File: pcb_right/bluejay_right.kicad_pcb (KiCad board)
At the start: 2 copper layers, 147 x 140.5 mm, 70 parts, among them J2 SJ-43514, U2 MCP23017

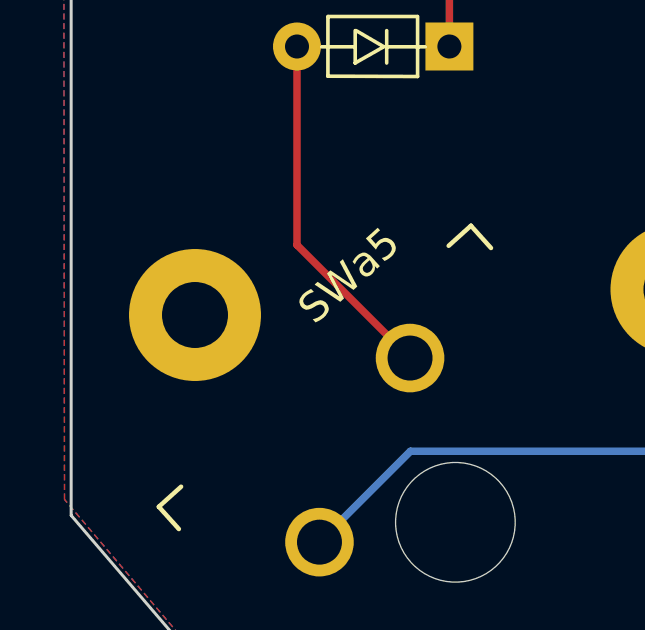
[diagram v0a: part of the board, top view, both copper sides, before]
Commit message: remove mounting hole 9
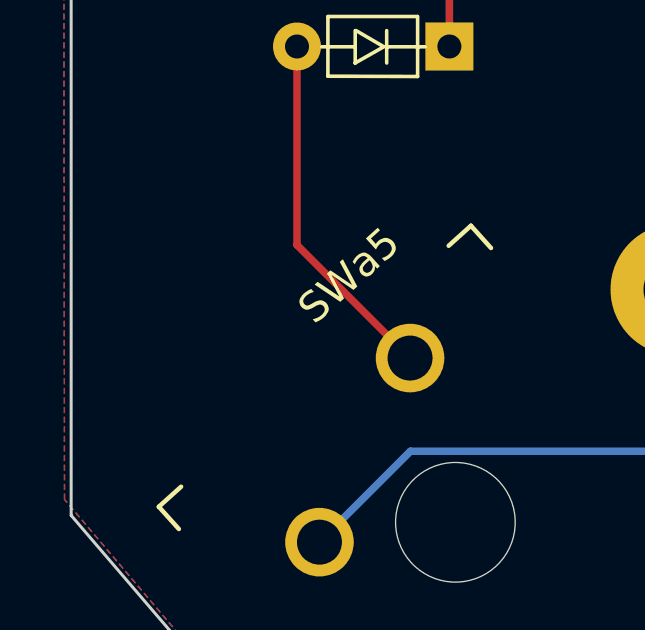
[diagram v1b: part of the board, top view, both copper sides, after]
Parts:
- removed H9: M2, MountingHole:MountingHole_2.2mm_M2_Pad
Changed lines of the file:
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@@
     )
-  )
-  (footprint "MountingHole:MountingHole_2.2mm_M2_Pad" (layer "F.Cu")
-    (at -56.95 64.15)
-    (descr "Mounting Hole 2.2mm, M2")
-    (tags "mounting hole 2.2mm m2")
-    (property "Sheetfile" "bluejay_right.kicad_sch")
-    (property "Sheetname" "")
-    (property "exclude_from_bom" "")
-    (attr exclude_from_pos_files exclude_from_bom)
-    (fp_text reference "H9" (at 0 -3.2) (layer "F.SilkS") hide
-      (effects (font (size 1 1) (thickness 0.15)))
-    )
-    (fp_text value "M2" (at 0 3.2) (layer "F.Fab")
-      (effects (font (size 1 1) (thickness 0.15)))
-    )
-    (fp_text user "${REFERENCE}" (at 0 0) (layer "F.Fab")
-      (effects (font (size 1 1) (thickness 0.15)))
-    )
-    (fp_circle (center 0 0) (end 2.2 0) (layer "Cmts.User") (width 0.15) (fill none))
-    (fp_circle (center 0 0) (end 2.45 0) (layer "F.CrtYd") (width 0.05) (fill none))
-    (pad "1" thru_hole circle (at 0 0) (size 4.4 4.4) (drill 2.2) (layers *.Cu *.Mask))
   )
   (footprint "BlueJay footprints:D_DO-35_SOD27_P5.08mm_Horizontal" (layer "F.Cu")

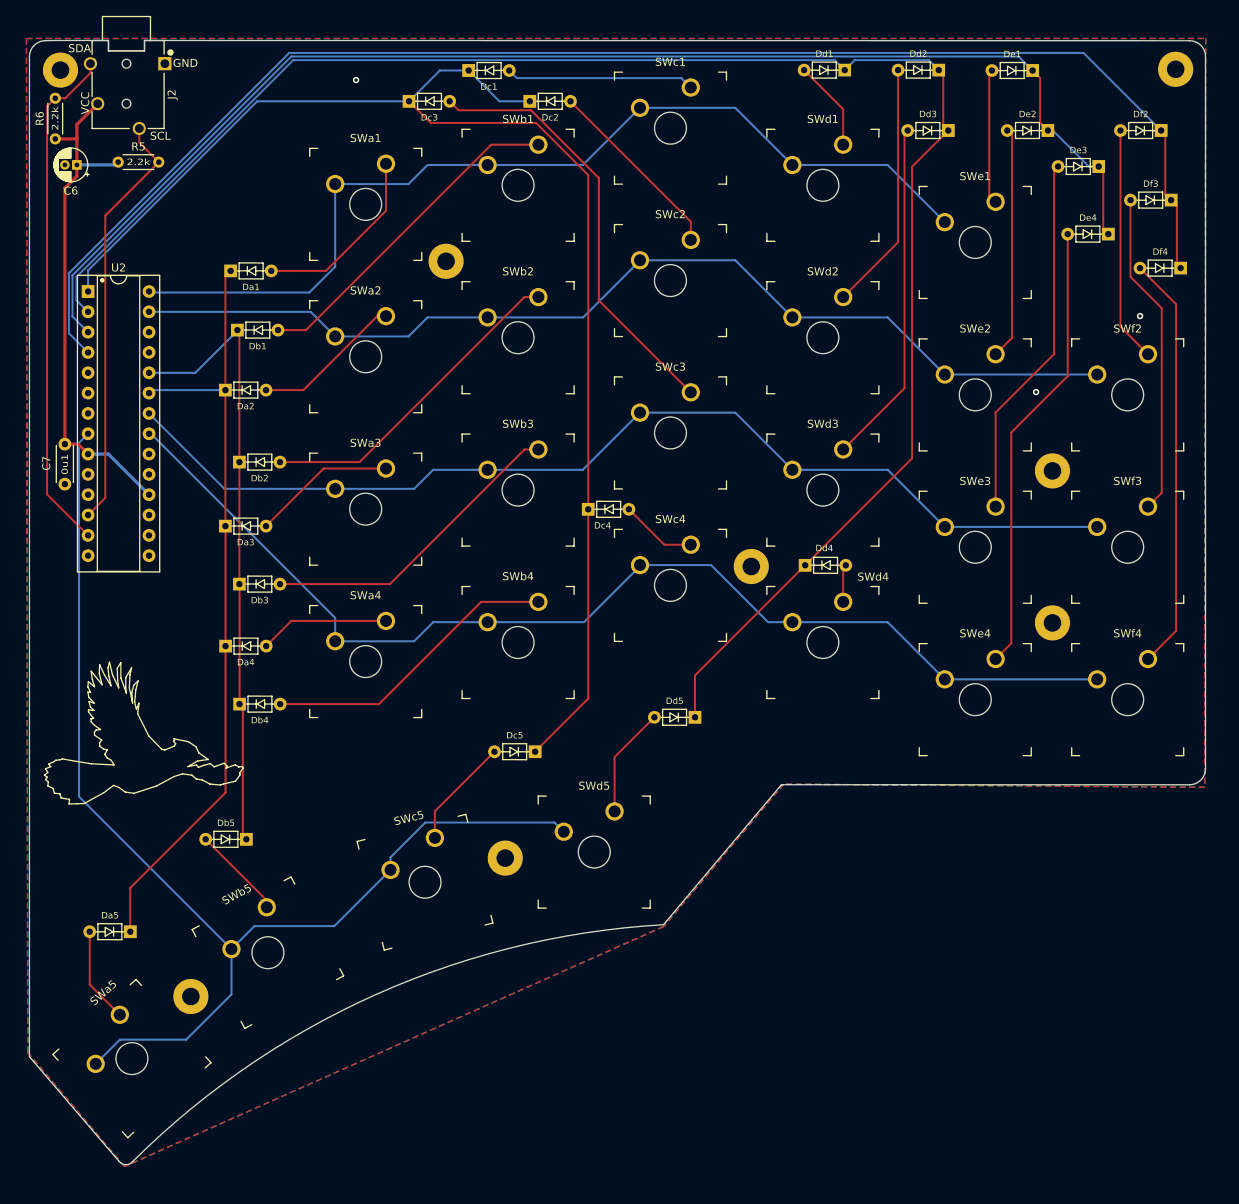
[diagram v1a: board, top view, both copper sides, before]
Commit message: Round edges of PCB
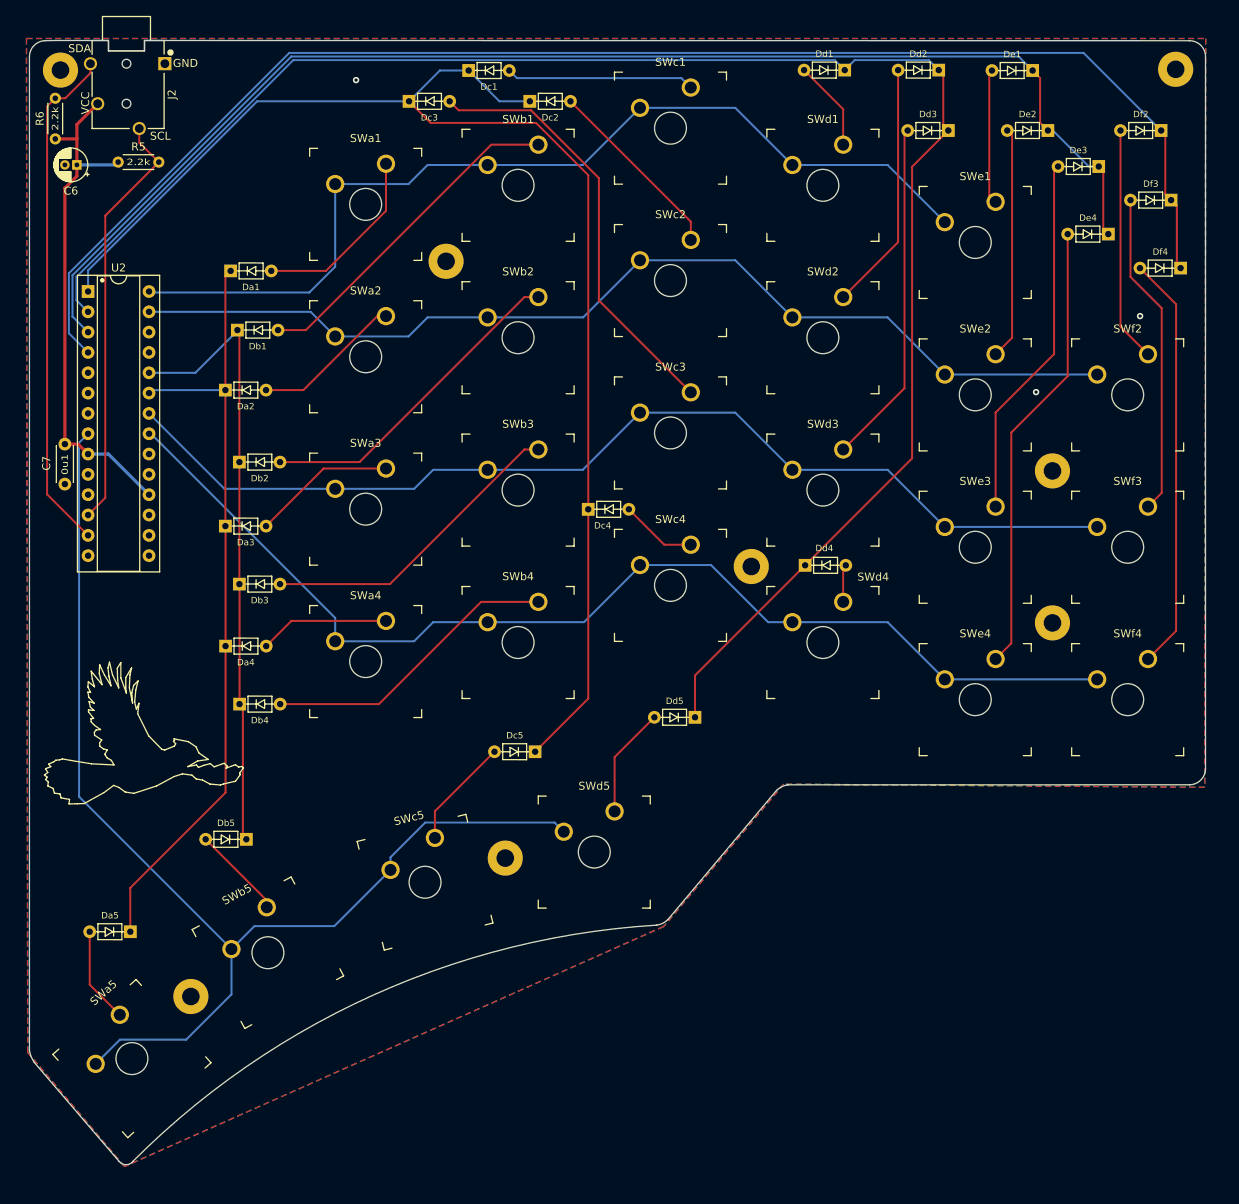
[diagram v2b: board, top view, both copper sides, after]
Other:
- outline, holes or cut-outs redrawn
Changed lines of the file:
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@@
   (gr_line locked (start -26.050003 -42.717995) (end -26.050003 -42.717995) (layer "Eco1.User") (width 0.188976))
   (gr_line locked (start 16.525009 38.243992) (end 16.525009 52.243992) (layer "Eco1.User") (width 0.188976))
+  (gr_arc (start -60.48 71.53) (mid -60.861151 70.823028) (end -61.075526 70.048994) (layer "Edge.Cuts") (width 0.1))
   (gr_line (start 85.928875 34.81) (end 85.927845 -54.17775) (layer "Edge.Cuts") (width 0.1))
   (gr_line (start -57.8 -56.2) (end -59.2 -56.175) (layer "Edge.Cuts") (width 0.1))
+  (gr_arc (start 32.311006 37.544474) (mid 32.96 37.08) (end 33.721006 36.844474) (layer "Edge.Cuts") (width 0.1))
   (gr_arc (start 85.928875 34.81) (mid 85.346563 36.23553) (end 83.928876 36.836717) (layer "Edge.Cuts") (width 0.1))
   (gr_arc (start -61.077843 -54.17) (mid -60.533214 -55.541811) (end -59.2 -56.175) (layer "Edge.Cuts") (width 0.1))
   (gr_line (start 83.927845 -56.17) (end -40.6 -56.2) (layer "Edge.Cuts") (width 0.1))
-  (gr_line (start -49.877844 83.9) (end -61.077844 70.83) (layer "Edge.Cuts") (width 0.1))
-  (gr_line (start 32.922156 36.83) (end 83.928876 36.836717) (layer "Edge.Cuts") (width 0.1))
-  (gr_arc (start -48.107844 83.87) (mid -48.985464 84.321423) (end -49.877844 83.9) (layer "Edge.Cuts") (width 0.1))
-  (gr_arc (start -48.107844 83.87) (mid -17.679753 63.015187) (end 18.172156 54.33) (layer "Edge.Cuts") (width 0.1))
-  (gr_line (start 18.172156 54.33) (end 32.922156 36.83) (layer "Edge.Cuts") (width 0.1))
-  (gr_line (start -61.077843 -54.17) (end -61.077844 70.83) (layer "Edge.Cuts") (width 0.1))
-  (gr_arc (start 83.927845 -56.17) (mid 85.346087 -55.593736) (end 85.927845 -54.17775) (layer "Edge.Cuts") (width 0.1))
+  (gr_line (start -49.877844 83.9) (end -60.48 71.53) (layer "Edge.Cuts") (width 0.1))
+  (gr_line (start 33.721006 36.844474) (end 83.928876 36.836717) (layer "Edge.Cuts") (width 0.1))
+  (gr_arc (start -48.107844 83.87) (mid -48.985447 84.321434) (end -49.877844 83.9) (layer "Edge.Cuts") (width 0.1))
+  (gr_arc (start -48.107844 83.87) (mid -18.100136 63.120872) (end 17.32 54.38) (layer "Edge.Cuts") (width 0.1))
+  (gr_line (start 18.73 53.68) (end 32.31 37.54) (layer "Edge.Cuts") (width 0.1))
+  (gr_line (start -61.077843 -54.17) (end -61.077844 70.05) (layer "Edge.Cuts") (width 0.1))
+  (gr_arc (start 83.927845 -56.17) (mid 85.346066 -55.593723) (end 85.927845 -54.17775) (layer "Edge.Cuts") (width 0.1))
+  (gr_arc (start 18.73 53.68) (mid 18.081006 54.144474) (end 17.32 54.38) (layer "Edge.Cuts") (width 0.1))
   (gr_text "BlueJay Keyboard rev 1.0" (at 84.81 30.37) (layer "B.SilkS")
     (effects (font (size 1 1) (thickness 0.15)) (justify left mirror))

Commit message: Update placement of some components and size of drill holes
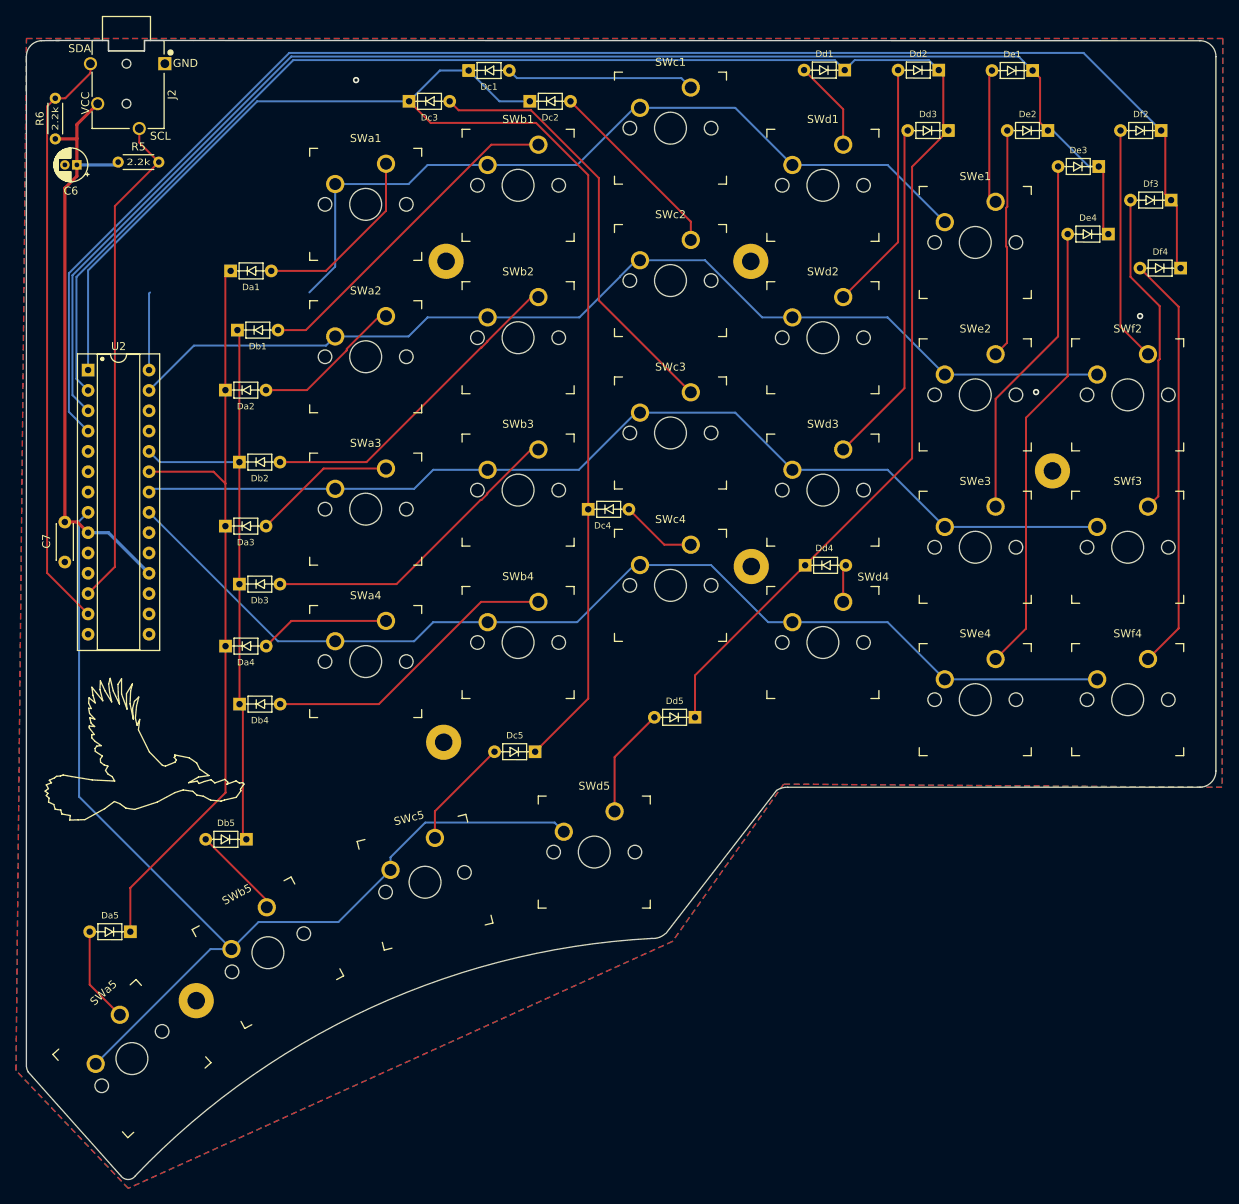
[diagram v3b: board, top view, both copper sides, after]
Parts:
- removed H7, H8: M2, MountingHole:MountingHole_2.2mm_M2_Pad
- C7: value 0u1 -> 100n
- SWa1, SWa2, SWa3, SWa4, SWa5, SWb1, SWb2, SWb3, SWb4, SWb5, SWc1, SWc2, SWc3, SWc4, SWc5, SWd1, SWd2, SWd3, SWd4, SWd5, SWe1, SWe2, SWe3, SWe4, SWf2, SWf3, SWf4: footprint BlueJay footprints:SW_MX_Plate -> BlueJay footprints:SW_MX
- moved H2 117.6 mm to (-40.2, 63.8)
- moved H6 77.5 mm to (-9.30, 31.5)
- moved H1 58.3 mm to (29.1, -28.6)
- moved U2 9.82 mm to (-53.8, -15.0)
- moved C7 9.74 mm to (-56.7, 3.99)
- moved G*** 2.02 mm to (-46.2, 36.0)
- moved H3 1.08 mm to (-9.00, -28.6)
- moved H5 0.55 mm to (29.1, 9.55)
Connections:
- H2 pad 1: GND -> (no net)
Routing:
- net /row5: track 148.5 -> 135.4 mm
- net /row1: track 121.0 -> 110.7 mm
- net /colF: track 181.1 -> 190.9 mm
- net /colE: track 165.4 -> 175.3 mm
- net /colC: track 170.9 -> 180.7 mm
- net /i2c_SDA: track 64.1 -> 73.9 mm
- net /i2c_SCL: track 53.0 -> 62.8 mm
- net /colD: track 220.7 -> 230.5 mm
- net VCC: track 65.4 -> 75.2 mm
- net /row4: track 140.9 -> 135.1 mm
- net /row3: track 132.3 -> 128.5 mm
- net /row2: track 129.7 -> 131.2 mm
- net /colB: track 77.4 -> 76.0 mm
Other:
- board size 147 x 140.5 mm -> 148.7 x 142.4 mm

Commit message: Fine tune edge cut
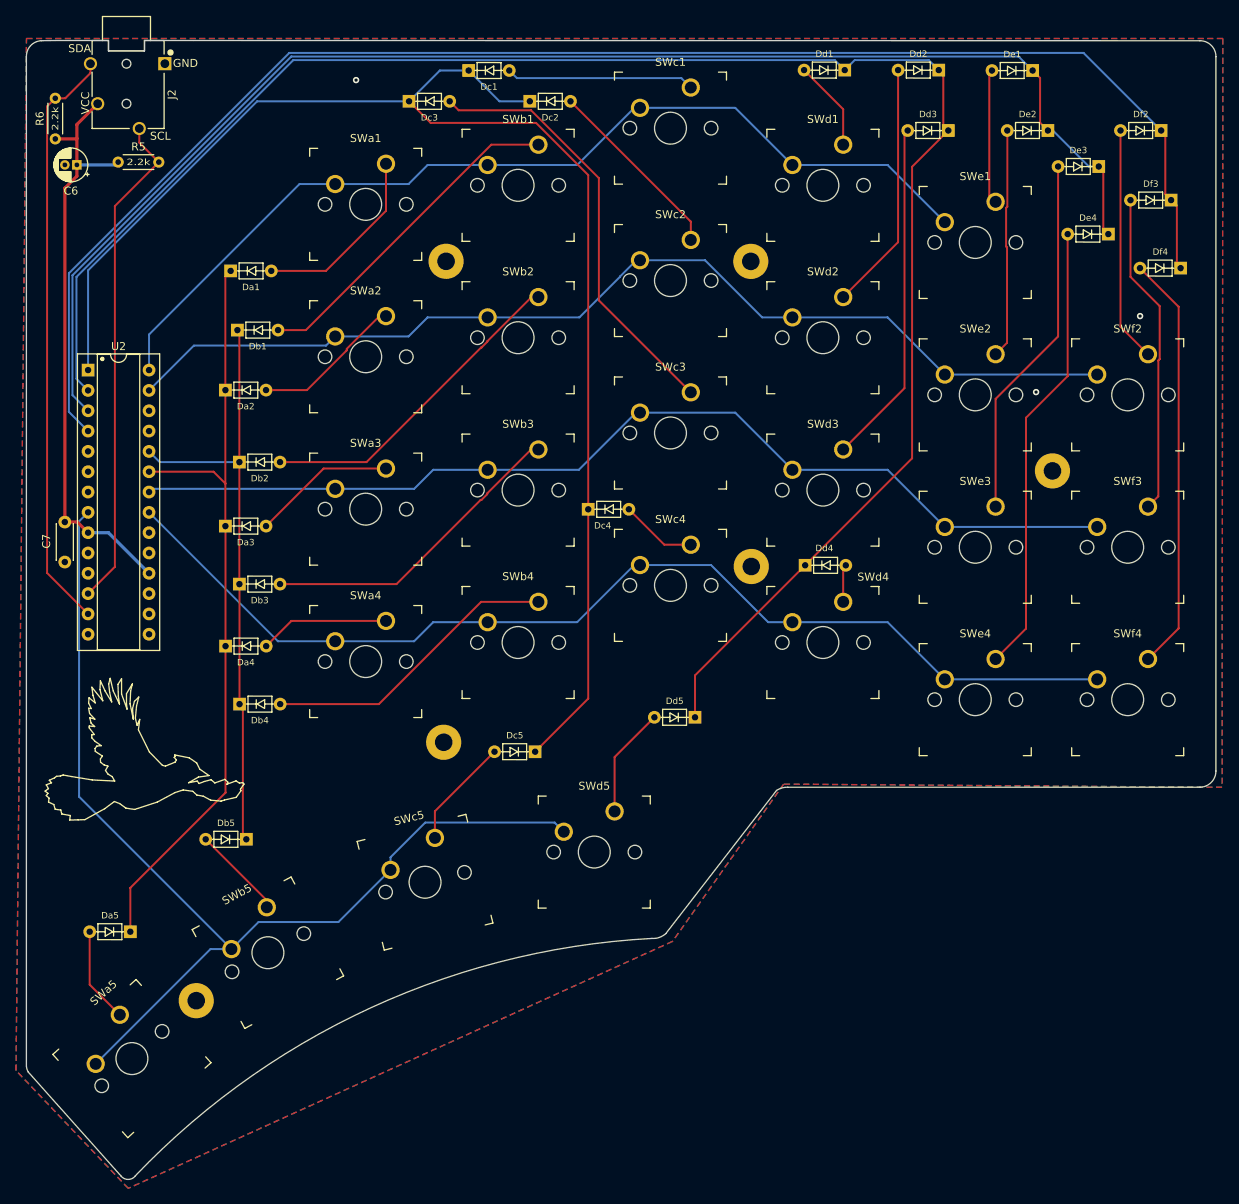
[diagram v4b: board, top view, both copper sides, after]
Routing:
- net /row1: track 110.7 -> 121.6 mm
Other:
- outline, holes or cut-outs redrawn
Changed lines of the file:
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@@
   (gr_arc (start -61.23 72.74) (mid -61.386012 72.382747) (end -61.46 72) (layer "Edge.Cuts") (width 0.1))
   (gr_line (start 87.23 35.11) (end 87.23 -54.18) (layer "Edge.Cuts") (width 0.1))
-  (gr_line (start -57.3 -56.2) (end -59.58 -56.175) (layer "Edge.Cuts") (width 0.1))
+  (gr_line (start -57.8 -56.2) (end -59.58 -56.175) (layer "Edge.Cuts") (width 0.1))
   (gr_arc (start 32.31 37.54) (mid 32.98386 37.23023) (end 33.72 37.14) (layer "Edge.Cuts") (width 0.1))
   (gr_arc (start 87.23 35.11) (mid 86.648353 36.53717) (end 85.23 37.14) (layer "Edge.Cuts") (width 0.1))
@@
   (gr_line (start -49.62 85.75) (end -61.23 72.74) (layer "Edge.Cuts") (width 0.1))
   (gr_line (start 33.72 37.14) (end 85.23 37.14) (layer "Edge.Cuts") (width 0.1))
-  (gr_arc (start -47.83 85.7) (mid -48.690274 86.173968) (end -49.59 85.78) (layer "Edge.Cuts") (width 0.1))
+  (gr_arc (start -47.83 85.7) (mid -48.712671 86.166365) (end -49.62 85.75) (layer "Edge.Cuts") (width 0.1))
   (gr_arc (start -47.83 85.7) (mid -18.380681 64.696706) (end 16.74 56.04) (layer "Edge.Cuts") (width 0.1))
   (gr_line (start 18.47 55.43) (end 32.31 37.54) (layer "Edge.Cuts") (width 0.1))
   (gr_line (start -61.46 -54.17) (end -61.46 72) (layer "Edge.Cuts") (width 0.1))
   (gr_arc (start 85.23 -56.17) (mid 86.647749 -55.594848) (end 87.23 -54.18) (layer "Edge.Cuts") (width 0.1))
-  (gr_arc (start 18.38 55.46) (mid 17.619397 55.917949) (end 16.74 56.04) (layer "Edge.Cuts") (width 0.1))
+  (gr_arc (start 18.47 55.43) (mid 17.667469 55.912166) (end 16.74 56.04) (layer "Edge.Cuts") (width 0.1))
   (gr_text "BlueJay Keyboard rev 1.0" (at 84.81 30.37) (layer "B.SilkS")
     (effects (font (size 1 1) (thickness 0.15)) (justify left mirror))
@@
   (segment (start -57.85 -48.98) (end -58.874511 -47.955489) (width 0.25) (layer "F.Cu") (net 37))
   (segment (start -58.874511 -47.955489) (end -58.874511 10.355489) (width 0.25) (layer "F.Cu") (net 37))
+  (segment (start -27.320222 -38.2588) (end -46.13 -19.449022) (width 0.25) (layer "B.Cu") (net 38))
   (segment (start 53.34 -33.4963) (end 46.1963 -40.64) (width 0.25) (layer "B.Cu") (net 38))
   (segment (start -3.81 -40.64) (end -11.31 -40.64) (width 0.25) (layer "B.Cu") (net 38))
   (segment (start 15.24 -47.7838) (end 14.5338 -47.7838) (width 0.25) (layer "B.Cu") (net 38))
+  (segment (start -46.13 -19.449022) (end -46.13 -15) (width 0.25) (layer "B.Cu") (net 38))
   (segment (start 14.5338 -47.7838) (end 7.39 -40.64) (width 0.25) (layer "B.Cu") (net 38))
-  (segment (start -46.005 -24.7) (end -46.13 -24.575) (width 0.25) (layer "B.Cu") (net 38))
   (segment (start -13.6912 -38.2588) (end -22.86 -38.2588) (width 0.25) (layer "B.Cu") (net 38))
-  (segment (start -46.13 -24.575) (end -46.13 -15) (width 0.25) (layer "B.Cu") (net 38))
-  (segment (start -22.86 -38.2588) (end -22.86 -27.94) (width 0.25) (layer "B.Cu") (net 38))
   (segment (start 34.29 -40.64) (end 27.1462 -47.7838) (width 0.25) (layer "B.Cu") (net 38))
   (segment (start 46.1963 -40.64) (end 34.29 -40.64) (width 0.25) (layer "B.Cu") (net 38))
-  (segment (start -22.86 -27.94) (end -26.1 -24.7) (width 0.25) (layer "B.Cu") (net 38))
   (segment (start 27.1462 -47.7838) (end 15.24 -47.7838) (width 0.25) (layer "B.Cu") (net 38))
   (segment (start 7.39 -40.64) (end -3.81 -40.64) (width 0.25) (layer "B.Cu") (net 38))
+  (segment (start -22.86 -38.2588) (end -27.320222 -38.2588) (width 0.25) (layer "B.Cu") (net 38))
   (segment (start -11.31 -40.64) (end -13.6912 -38.2588) (width 0.25) (layer "B.Cu") (net 38))
   (segment (start 7.66 -21.59) (end -3.81 -21.59) (width 0.25) (layer "B.Cu") (net 39))
